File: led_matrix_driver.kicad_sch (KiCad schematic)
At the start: 25 parts, among them J2 Screw_Terminal_01x02, J3 Screw_Terminal_01x02, J4 Conn_01x06_Pin, J5 Conn_02x17_Odd_Even, SW1 CK KMS221GPLFS, SW2 CK KMS221GPLFS, U2 Pico, U3 ESP32-WROOM-32, U4 AP1117-33, U6 Teensy4.0, U7 74AHCT541, U8 74AHCT541

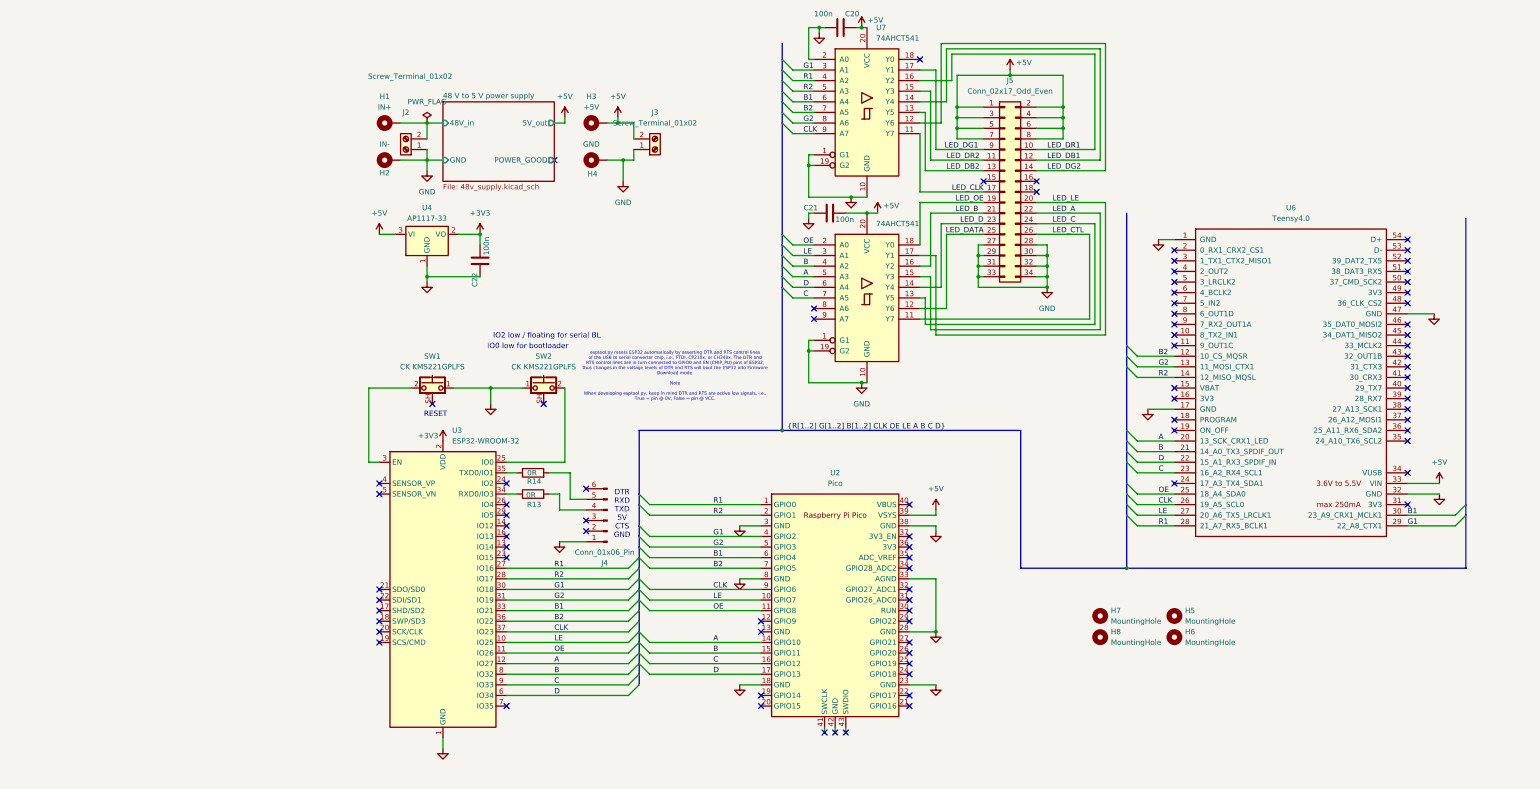
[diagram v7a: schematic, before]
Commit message: Minor updates and JLCPCB component codes added
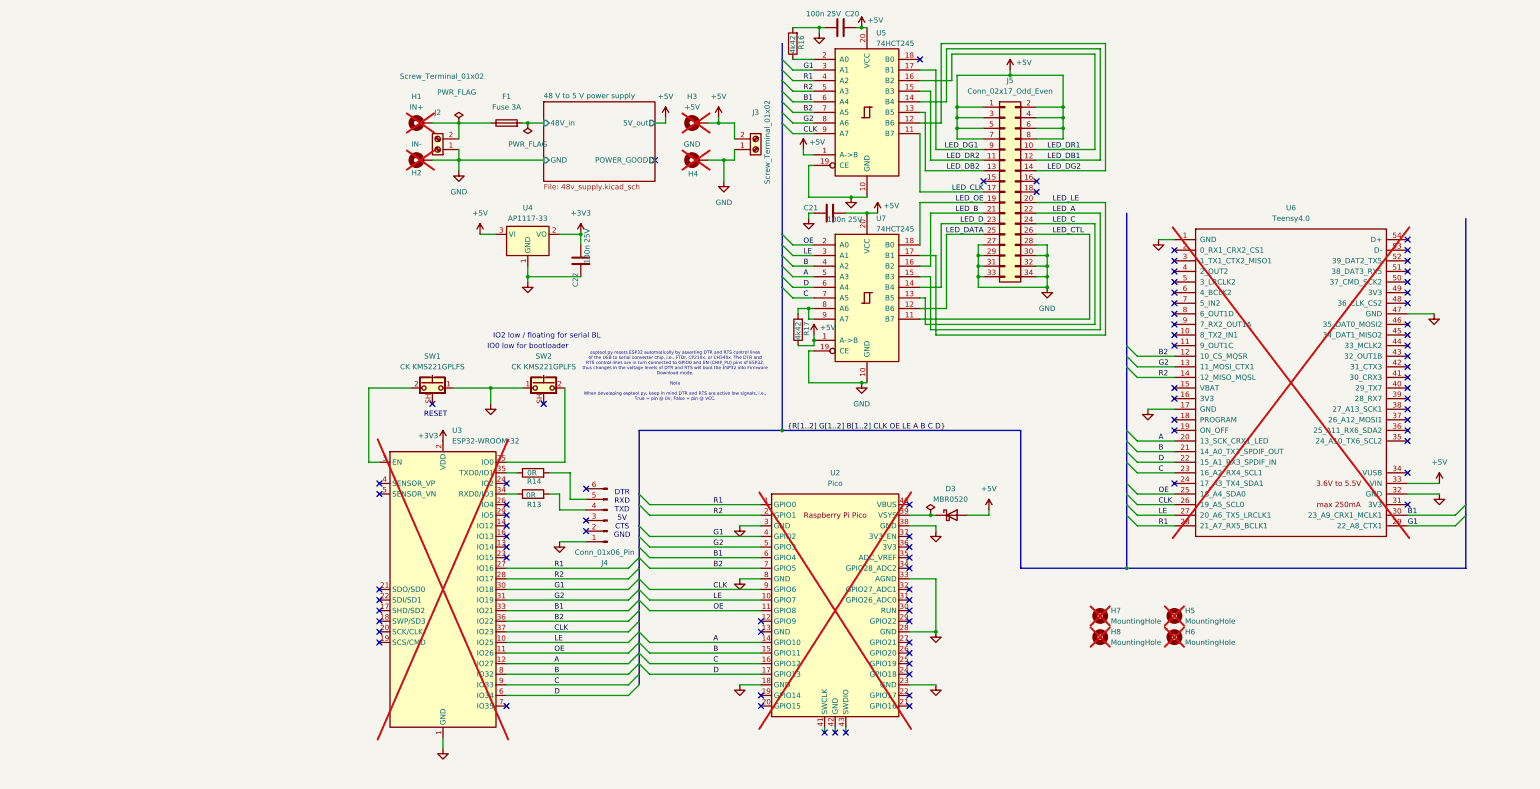
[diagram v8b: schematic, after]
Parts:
- removed U7, U8: 74AHCT541, Package_SO:SOIC-20W_7.5x12.8mm_P1.27mm, symbol 74xx:74AHCT541
- added D3: MBR0520, Diode_SMD:D_SOD-123, symbol Device:D_Schottky
- added F1: Fuse 3A, Fuse:Fuseholder_Littelfuse_Nano2_154x, symbol Device:Fuse
- added R16, R17: 4k42, Resistor_SMD:R_0603_1608Metric, symbol Device:R
- added U5, U7: 74HCT245, Package_SO:SOIC-20W_7.5x12.8mm_P1.27mm, symbol 74xx:74HC245
- C20, C21, C22: value 100n -> 100n 25V; footprint Capacitor_SMD:C_0603_1608Metric -> Capacitor_SMD:C_0805_2012Metric; DK 1276-1006-1-ND -> 478-KGM21NR71E104KTCT-ND; LCSC (none) -> C28233
- H1, H2, H3, H4, H5, H6, H7, H8, U2, U3, U6: now not fitted
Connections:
- net +5V: now also D3.2 (A), R17.1, U5.1 (A->B), U5.20 (VCC), U7.1 (A->B), U7.20 (VCC); no longer U2.39 (VSYS)
- net 48 V to 5 V power supply/48V_in: now also F1.2; no longer H1.1, J2.2 (Pin_2)
- net A: now also U7.5 (A3)
- net B: now also U7.4 (A2)
- net B1: now also U5.6 (A4)
- net B2: now also U5.7 (A5)
- net C: now also U7.7 (A5)
- net CLK: now also U5.9 (A7)
- net D: now also U7.6 (A4)
- net G1: now also U5.3 (A1)
- net G2: now also U5.8 (A6)
- net GND: now also R16.2, U5.10 (GND), U5.19 (CE), U7.10 (GND), U7.19 (CE)
- net LE: now also U7.3 (A1)
- net LED_A: now also U7.15 (B3)
- net LED_B: now also U7.16 (B2)
- net LED_C: now also U7.13 (B5)
- net LED_CLK: now also U5.11 (B7)
- net LED_CTL: now also U7.11 (B7)
- net LED_D: now also U7.14 (B4)
- net LED_DATA: now also U7.12 (B6)
- net LED_DB1: now also U5.14 (B4)
- net LED_DB2: now also U5.13 (B5)
- net LED_DG1: now also U5.17 (B1)
- net LED_DG2: now also U5.12 (B6)
- net LED_DR1: now also U5.16 (B2)
- net LED_DR2: now also U5.15 (B3)
- net LED_LE: now also U7.17 (B1)
- net LED_OE: now also U7.18 (B0)
- net OE: now also U7.2 (A0)
- net R1: now also U5.4 (A2)
- net R2: now also U5.5 (A3)
- new net: F1.1, H1.1, J2.2 (Pin_2)
- new net: R16.1, U5.2 (A0)
- new net: R17.2, U7.8 (A6), U7.9 (A7)
- new net: D3.1 (K), U2.39 (VSYS)
- no-connect marks 86 -> 84
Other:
- moved on the sheet: C22, J2, J3, U4
